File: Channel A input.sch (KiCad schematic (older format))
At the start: 21 parts, among them J11 Conn_01x10, J2 MJ-3523-SMT-TR, J6 Conn_01x02, P2 100k, SW2 SW_SPDT, U3 TL072

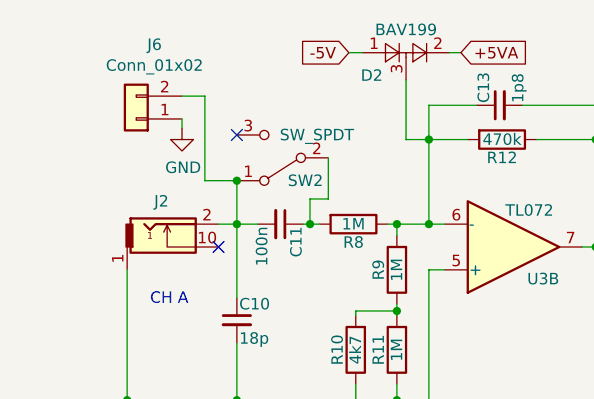
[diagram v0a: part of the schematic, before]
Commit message: fixed schematic and updated PCB
Fixed the schematic after having found the issues in the GBDSO schematic (which is also fixed on the repo).
Continued making the PCB for the modules. We're not at 7 modules from 10.
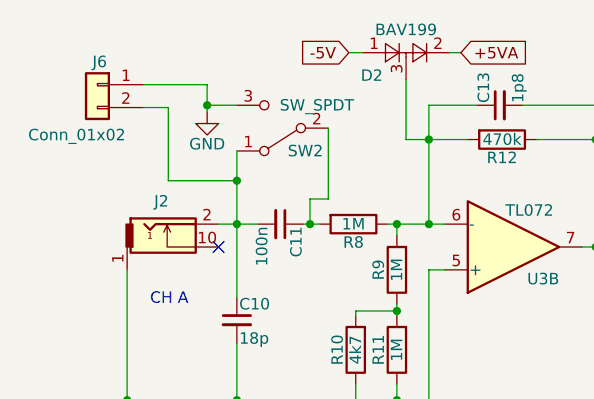
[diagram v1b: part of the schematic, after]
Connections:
- net GND: now also SW2.3 (C)
- no-connect marks 3 -> 2
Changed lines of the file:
@@
-$EndComp
-$Comp
-L Switch:SW_SPDT SW?
-U 1 1 5F958E74
-P 1830 1460
-AR Path="/5F958E74" Ref="SW?"  Part="1"
-AR Path="/5F6C55C3/5F958E74" Ref="SW?"  Part="1"
-AR Path="/5F6C8F99/5F958E74" Ref="SW2"  Part="1"
-F 0 "SW2" H 1730 1560 50  0000 C CNN
-F 1 "SW_SPDT" H 1680 1360 50  0000 C CNN
-F 2 "Button_Switch_SMD:SW_SPDT_CK-JS102011SAQN" H 1830 1460 50  0001 C CNN
-F 3 "" H 1830 1460 50  0001 C CNN
-	1    1830 1460
-	-1   0    0    1
 $EndComp
 $Comp
@@
 Connection ~ 1150 2520
 Wire Wire Line
-	1630 1560 1630 1750
-Wire Wire Line
-	2030 1460 2030 1640
-Wire Wire Line
 	2030 1640 1950 1640
 Wire Wire Line
@@
 	2330 2130 2330 2100
 Connection ~ 2330 2130
-NoConn ~ 1630 1360
-$Comp
-L Connector_Generic:Conn_01x02 J?
-U 1 1 5F958EE1
-P 1190 1290
-AR Path="/5F958EE1" Ref="J?"  Part="1"
-AR Path="/5F6C55C3/5F958EE1" Ref="J?"  Part="1"
-AR Path="/5F6C8F99/5F958EE1" Ref="J6"  Part="1"
-F 0 "J6" H 1110 965 50  0000 C CNN
-F 1 "Conn_01x02" H 1110 1056 50  0000 C CNN
-F 2 "Connector_PinHeader_2.54mm:PinHeader_1x02_P2.54mm_Horizontal" H 1190 1290 50  0001 C CNN
-F 3 "~" H 1190 1290 50  0001 C CNN
-	1    1190 1290
-	-1   0    0    1
-$EndComp
-Wire Wire Line
-	1630 1560 1490 1560
-Wire Wire Line
-	1490 1560 1490 1190
-Wire Wire Line
-	1490 1190 1390 1190
-Connection ~ 1630 1560
-$Comp
-L power:GND #PWR?
-U 1 1 5F958EEB
-P 1390 1330
-AR Path="/5F6C55C3/5F958EEB" Ref="#PWR?"  Part="1"
-AR Path="/5F6C8F99/5F958EEB" Ref="#PWR0110"  Part="1"
-F 0 "#PWR0110" H 1390 1080 50  0001 C CNN
-F 1 "GND" H 1395 1157 50  0000 C CNN
-F 2 "" H 1390 1330 50  0001 C CNN
-F 3 "" H 1390 1330 50  0001 C CNN
-	1    1390 1330
-	1    0    0    -1
-$EndComp
-Wire Wire Line
-	1390 1290 1390 1330
 Text Notes 1250 2110 0    50   ~ 0
 CH A
@@
 Text GLabel 3920 3300 0    50   Output ~ 0
 DPOT_1H
+Wire Wire Line
+	1330 1240 1220 1240
+Wire Wire Line
+	1330 1560 1330 1240
+Connection ~ 1500 1230
+Wire Wire Line
+	1500 1140 1500 1230
+Wire Wire Line
+	1220 1140 1500 1140
+Wire Wire Line
+	1500 1230 1630 1230
+Wire Wire Line
+	1500 1260 1500 1230
+$Comp
+L power:GND #PWR?
+U 1 1 5E8A92A9
+P 1500 1260
+AR Path="/5F6C55C3/5E8A92A9" Ref="#PWR?"  Part="1"
+AR Path="/5F6C72AE/5E8A92A9" Ref="#PWR?"  Part="1"
+AR Path="/5F6C8F99/5E8A92A9" Ref="#PWR0110"  Part="1"
+F 0 "#PWR0110" H 1500 1010 50  0001 C CNN
+F 1 "GND" H 1500 1120 50  0000 C CNN
+F 2 "" H 1500 1260 50  0001 C CNN
+F 3 "" H 1500 1260 50  0001 C CNN
+	1    1500 1260
+	1    0    0    -1
+$EndComp
+$Comp
+L Connector_Generic:Conn_01x02 J?
+U 1 1 5E8A92A3
+P 1020 1140
+AR Path="/5E8A92A3" Ref="J?"  Part="1"
+AR Path="/5F6C55C3/5E8A92A3" Ref="J?"  Part="1"
+AR Path="/5F6C72AE/5E8A92A3" Ref="J?"  Part="1"
+AR Path="/5F6C8F99/5E8A92A3" Ref="J6"  Part="1"
+F 0 "J6" H 1010 1240 50  0000 C CNN
+F 1 "Conn_01x02" H 1110 920 50  0000 C CNN
+F 2 "Connector_PinHeader_2.54mm:PinHeader_1x02_P2.54mm_Horizontal" H 1020 1140 50  0001 C CNN
+F 3 "~" H 1020 1140 50  0001 C CNN
+	1    1020 1140
+	-1   0    0    -1
+$EndComp
+$Comp
+L Switch:SW_SPDT SW?
+U 1 1 5E8A929B
+P 1830 1330
+AR Path="/5E8A929B" Ref="SW?"  Part="1"
+AR Path="/5F6C55C3/5E8A929B" Ref="SW?"  Part="1"
+AR Path="/5F6C72AE/5E8A929B" Ref="SW?"  Part="1"
+AR Path="/5F6C8F99/5E8A929B" Ref="SW2"  Part="1"
+F 0 "SW2" H 1730 1430 50  0000 C CNN
+F 1 "SW_SPDT" H 1680 1230 50  0000 C CNN
+F 2 "Button_Switch_SMD:SW_SPDT_CK-JS102011SAQN" H 1830 1330 50  0001 C CNN
+F 3 "" H 1830 1330 50  0001 C CNN
+	1    1830 1330
+	-1   0    0    1
+$EndComp
+Wire Wire Line
+	1330 1560 1630 1560
+Wire Wire Line
+	1630 1430 1630 1560
+Connection ~ 1630 1560
+Wire Wire Line
+	1630 1560 1630 1750
+Wire Wire Line
+	2030 1330 2030 1640
 $EndSCHEMATC
